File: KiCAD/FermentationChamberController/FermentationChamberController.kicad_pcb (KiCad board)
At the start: 2 copper layers, 43.2 x 17.8 mm, 18 parts, among them J1 Screw_Terminal_1x02, J2 Screw_Terminal_1x02, J3 Screw_Terminal_1x02, J4 CONN_01X04, J5 CONN_01X04, P1 Digital, P2 Analog, Q1 TIP120, Q2 TIP120, SW1 Rotary_Encoder_Switch

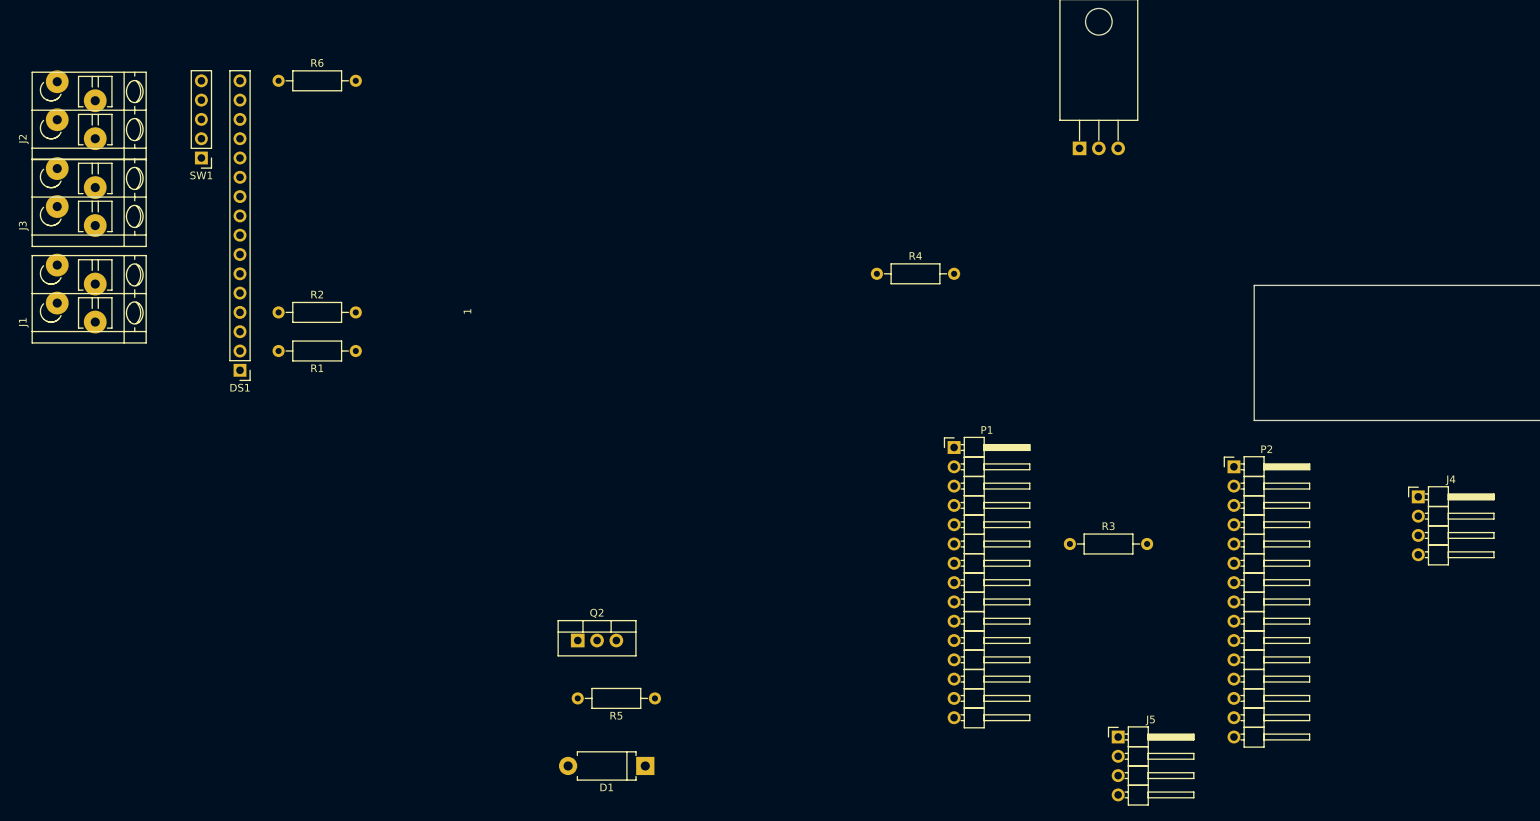
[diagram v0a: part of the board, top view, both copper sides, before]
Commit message: Updated header styles for the arduino, fan and relay connectors.
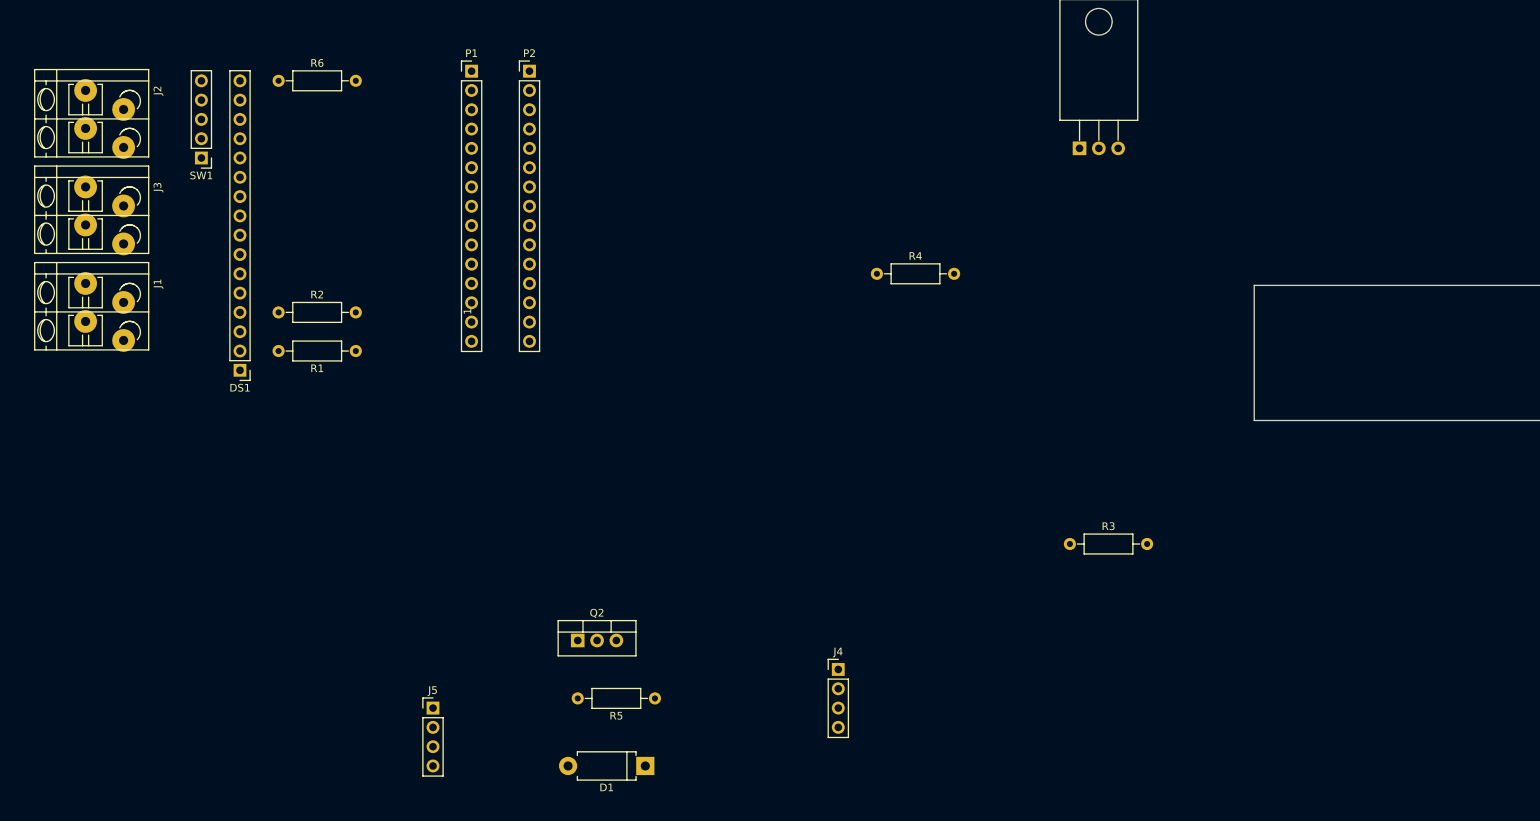
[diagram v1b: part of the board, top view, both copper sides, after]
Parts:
- J4, J5: footprint Pin_Headers:Pin_Header_Angled_1x04_Pitch2.54mm -> Pin_Headers:Pin_Header_Straight_1x04_Pitch2.54mm
- P1, P2: footprint Pin_Headers:Pin_Header_Angled_1x15_Pitch2.54mm -> Pin_Headers:Pin_Header_Straight_1x15_Pitch2.54mm
- moved P2 106.3 mm to (138.4, 64.8)
- moved J5 90.3 mm to (125.7, 148.6)
- moved P1 80.5 mm to (130.8, 64.8)
- moved J4 79.6 mm to (179.1, 143.5)
- moved J2 6.48 mm to (80.0, 67.3), turned to 270 degrees
- moved J1 5.24 mm to (80.0, 92.7), turned to 270 degrees
- moved J3 5.24 mm to (80.0, 80.0), turned to 270 degrees

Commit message: Updated PCB layour
almost done.... maybe
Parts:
- added REF**: To Arduino Board, Pin_Headers:Pin_Header_Straight_2x04_Pitch2.54mm, F.Cu at (73.7, 78.7)
- added REF**: To Relay Board, Pin_Headers:Pin_Header_Straight_2x04_Pitch2.54mm, F.Cu at (41.9, 58.4)
- J1: value Screw_Terminal_1x02 -> G Vcc; footprint Connectors_Terminal_Blocks:TerminalBlock_WAGO-804_RM5mm_2pol -> Connectors:bornier2
- J2: value Screw_Terminal_1x02 -> 1Wire 1Wire; footprint Connectors_Terminal_Blocks:TerminalBlock_WAGO-804_RM5mm_2pol -> Connectors:bornier2
- J3: value Screw_Terminal_1x02 -> Vcc G; footprint Connectors_Terminal_Blocks:TerminalBlock_WAGO-804_RM5mm_2pol -> Connectors:bornier2
- J4: value CONN_01X04 -> Relay Connection
- J5: value CONN_01X04 -> Fan
- SW1: value Rotary_Encoder_Switch -> A C B S1 S2
- moved R3 179.6 mm to (59.7, 27.9), turned to 270 degrees
- moved Q1 170.6 mm to (43.2, 43.2)
- moved R4 148.6 mm to (41.9, 48.3)
- moved J4 119.9 mm to (73.7, 86.4), turned to 90 degrees
- moved D1 110.1 mm to (68.6, 86.4)
- moved R5 109.5 mm to (68.6, 80.0)
- moved Q2 106.7 mm to (61.0, 73.7)
- moved J5 103.3 mm to (52.1, 76.2)
- moved R1 99.1 mm to (35.6, 43.2), turned to 270 degrees
- moved J1 82.9 mm to (26.7, 29.2), turned to 90 degrees
- moved DS1 80.1 mm to (97.8, 24.1), turned to 270 degrees
- moved P2 77.7 mm to (61.0, 58.4), turned to 90 degrees
- moved P1 73.1 mm to (61.0, 43.2), turned to 90 degrees
- moved R2 68.5 mm to (92.7, 29.2), turned to 180 degrees
- moved R6 62.5 mm to (55.9, 27.9), turned to 270 degrees
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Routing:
- net /10(**/SS): track 0.00 -> 85.1 mm, vias 0 -> 2
- net /13(SCK): track 0.00 -> 49.4 mm, vias 0 -> 2
- net /A3: track 0.00 -> 43.4 mm
- net /A0: track 0.00 -> 36.4 mm
- net /A1: track 0.00 -> 33.3 mm
- net /A2: track 0.00 -> 30.3 mm
- net /9(**): track 0.00 -> 29.6 mm, vias 0 -> 2
- net /11(**/MOSI): track 0.00 -> 29.2 mm
- net Net-(DS1-Pad16): track 0.00 -> 27.8 mm
- net /4: track 0.00 -> 27.5 mm
- net /5(**): track 0.00 -> 26.0 mm
- net /6(**): track 0.00 -> 25.3 mm
- net /7: track 0.00 -> 23.8 mm
- net /8: track 0.00 -> 23.2 mm
- net /12(MISO): track 0.00 -> 21.7 mm
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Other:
- board size 43.2 x 17.8 mm -> 87.6 x 48.3 mm
- board text removed: "1"

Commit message: Updates to Kicad and testing
RJ 45 connectors
bad test for wifi...
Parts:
- removed REF**: To Arduino Board, Pin_Headers:Pin_Header_Straight_2x04_Pitch2.54mm
- removed REF**: To Relay Board, Pin_Headers:Pin_Header_Straight_2x04_Pitch2.54mm
- added J6: CONN_01X08, Connectors:RJ45_8, F.Cu at (35.6, 59.7)
- added J7: CONN_01X08, Connectors:RJ45_8, F.Cu at (82.5, 85.1)
- added J8: DC Power Supply, Pin_Headers:Pin_Header_Straight_1x02_Pitch1.27mm, F.Cu at (50.8, 86.4)
- J4: value Relay Connection -> CONN_01X04
- J5: value Fan -> CONN_01X04
- SW1: value A C B S1 S2 -> Rotary_Encoder_Switch
- moved J5 2.84 mm to (50.8, 73.7)
- moved Q2 1.80 mm to (59.7, 74.9)
- moved D1 1.80 mm to (67.3, 87.6)
- moved J4 1.80 mm to (72.4, 87.6), turned to 180 degrees
- moved R5 1.80 mm to (67.3, 81.3)
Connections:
- J4 pad 2: /A2 -> Net-(J4-Pad2)
- J4 pad 3: /A1 -> Net-(J4-Pad3)
- J5 pad 1: /2 -> Net-(J5-Pad1)
- J5 pad 2: /9(**) -> Net-(J5-Pad2)
- P2 pad 1: /Vin -> +12V
- R5 pad 1: /A0 -> Net-(J7-Pad8)
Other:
- board size 87.6 x 48.3 mm -> 87.6 x 45.7 mm
